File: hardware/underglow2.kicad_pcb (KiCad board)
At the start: 4 copper layers, 6 parts, among them U201 TPS62172DSGR

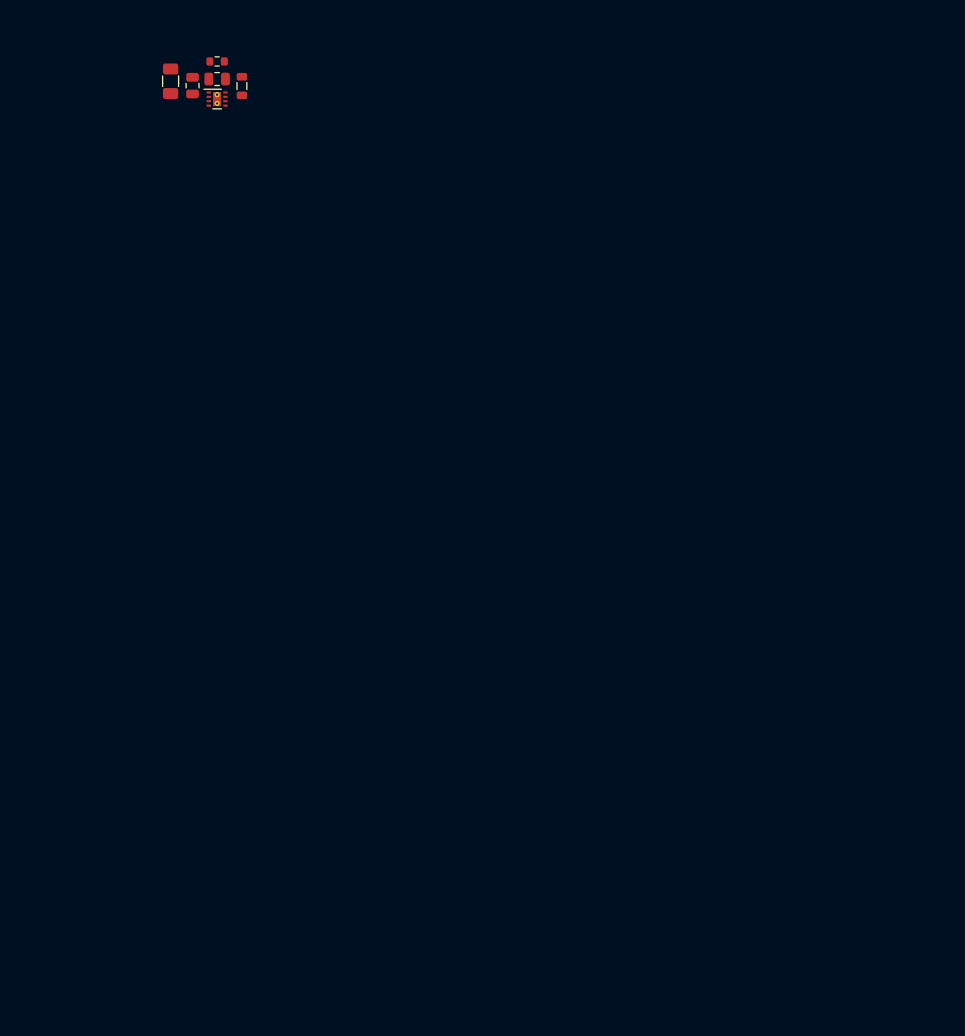
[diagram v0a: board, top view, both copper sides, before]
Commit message: Schematic updates: stm32 sheet
Signed-off-by: Connor Rigby <connorr@hey.com>
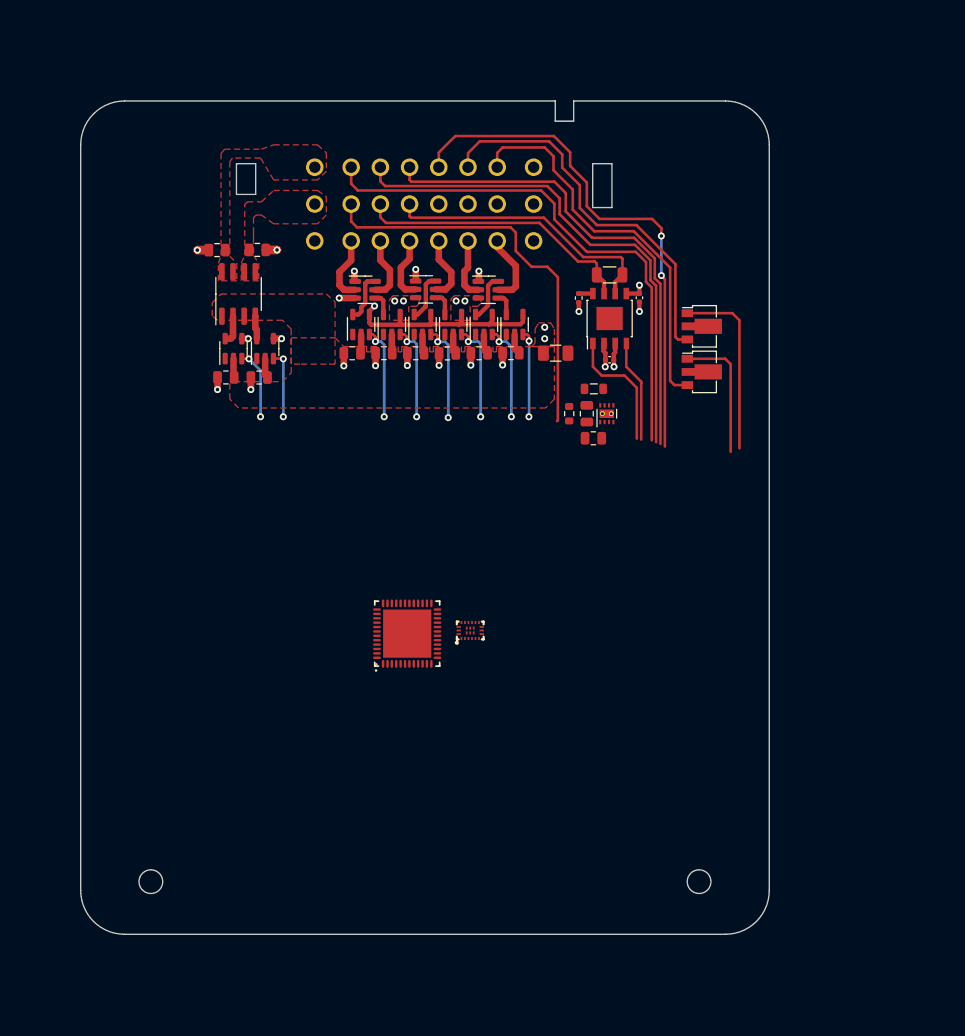
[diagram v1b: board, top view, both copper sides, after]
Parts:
- added C301: C_0805_10u_X5R, Capacitor_SMD:C_0805_2012Metric, F.Cu at (59.6, 53.8)
- added C302: C_0805_10u_X5R, Capacitor_SMD:C_0805_2012Metric, F.Cu at (56.0, 53.8)
- added C303: C_0805_10u_X5R, Capacitor_SMD:C_0805_2012Metric, F.Cu at (66.8, 53.8)
- added C304: C_0805_10u_X5R, Capacitor_SMD:C_0805_2012Metric, F.Cu at (63.2, 53.8)
- added C305: C_0805_10u_X5R, Capacitor_SMD:C_0805_2012Metric, F.Cu at (74.0, 53.8)
- added C306: C_0805_10u_X5R, Capacitor_SMD:C_0805_2012Metric, F.Cu at (70.4, 53.8)
- added C307: C_0805_10u_X5R, Capacitor_SMD:C_0805_2012Metric, F.Cu at (41.5, 56.5)
- added C308: C_0805_10u_X5R, Capacitor_SMD:C_0805_2012Metric, F.Cu at (45.4, 56.5)
- added C309: C_0805_10u_X5R, Capacitor_SMD:C_0805_2012Metric, F.Cu at (40.5, 42.0)
- added C310: C_0805_10u_X5R, Capacitor_SMD:C_0805_2012Metric, F.Cu at (45.1, 42.0)
- added C401: C_0402_100nf_X7R, Capacitor_SMD:C_0402_1005Metric, F.Cu at (85.3, 54.5)
- added C402: C_0402_100nf_X7R, Capacitor_SMD:C_0402_1005Metric, F.Cu at (88.7, 47.4)
- added H1101: MountingHole_Pad, MountingHole:MountingHole_2.7mm_M2.5, F.Cu at (33.0, 114.0)
- added H1102: MountingHole_Pad, MountingHole:MountingHole_2.7mm_M2.5, F.Cu at (95.5, 114.0)
- added J101: J_Delphi_Sicma_24, bom:Delphi_Sicma_24_Black, F.Cu at (64.2, 25.0)
- added Q301: AO4803A, Package_SO:SOP-8_3.76x4.96mm_P1.27mm, F.Cu at (43.0, 47.0)
- added Q302: 8205A, Package_TO_SOT_SMD:SOT-23-6, F.Cu at (57.4, 46.5)
- added Q303: 8205A, Package_TO_SOT_SMD:SOT-23-6, F.Cu at (64.3, 46.5)
- added Q304: 8205A, Package_TO_SOT_SMD:SOT-23-6, F.Cu at (71.5, 46.5)
- added Q305: BCX56, Package_TO_SOT_SMD:SOT-89-3, F.Cu at (95.8, 55.9)
- added Q306: BCX56, Package_TO_SOT_SMD:SOT-89-3, F.Cu at (95.8, 50.7)
- added R401: R_1206_120, Resistor_SMD:R_1206_3216Metric, F.Cu at (85.3, 44.8)
- added R402: R_0402_10k, Resistor_SMD:R_0402_1005Metric, F.Cu at (81.8, 47.5)
- added U301: MCP1416, Package_TO_SOT_SMD:SOT-23-5, F.Cu at (60.5, 50.5)
- added U302: MCP1416, Package_TO_SOT_SMD:SOT-23-5, F.Cu at (57.0, 50.5)
- added U303: MCP1416, Package_TO_SOT_SMD:SOT-23-5, F.Cu at (67.5, 50.5)
- added U304: MCP1416, Package_TO_SOT_SMD:SOT-23-5, F.Cu at (64.0, 50.5)
- added U305: MCP1416, Package_TO_SOT_SMD:SOT-23-5, F.Cu at (74.5, 50.5)
- added U306: MCP1416, Package_TO_SOT_SMD:SOT-23-5, F.Cu at (71.0, 50.5)
- added U307: MCP1416, Package_TO_SOT_SMD:SOT-23-5, F.Cu at (42.4, 53.2)
- added U308: MCP1416, Package_TO_SOT_SMD:SOT-23-5, F.Cu at (46.0, 53.2)
- added U401: TLE9251VSJXUMA1, Package_SO:Infineon_PG-DSO-8-43, F.Cu at (85.3, 49.8)
- added U501: STM32G431CBU6, LCSC_Microcontroller:UFQFPN-48_L7.0-W7.0-P0.50-BL-EP, F.Cu at (62.2, 85.7)
- added U601: DA14531-00000FX2, LCSC_Microcontroller:FCGQFN-24_L3.0-W2.2-P0.40-BL, F.Cu at (69.4, 85.4)
- moved C201 60.9 mm to (83.4, 63.5), turned to 180 degrees
- moved U201 57.1 mm to (85.0, 60.6), turned to 90 degrees
- moved C202 56.9 mm to (82.7, 60.6), turned to -90 degrees
- moved R203 56.8 mm to (80.7, 60.6), turned to -90 degrees
- moved F201 53.7 mm to (79.2, 53.8), turned to 0 degrees
- moved L201 52.9 mm to (83.5, 57.8), turned to 180 degrees
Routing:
- net /Digital Input/DI_1: track 0.00 -> 60.8 mm
- net /Digital Input/DI_4: track 0.00 -> 59.7 mm, vias 0 -> 2
- net /Digital Input/DI_2: track 0.00 -> 58.2 mm
- net /Digital Input/DI_3: track 0.00 -> 55.8 mm
- net GND: track 0.00 -> 50.6 mm, vias 0 -> 24
- net /Power/EN: track 0.00 -> 45.9 mm
- net /RGB/PIXEL_1: track 0.00 -> 44.6 mm
- net /RGB/PIXEL_2: track 0.00 -> 43.8 mm
- net /CAN/CAN_H: track 0.00 -> 32.1 mm
- net /CAN/CAN_L: track 0.00 -> 32.0 mm
- net /Application/PIXEL_2_PWM: track 0.00 -> 20.9 mm
- net +12V: track 0.00 -> 17.9 mm, vias 0 -> 2
- net /Application/PIXEL_1_PWM: track 0.00 -> 15.2 mm
- net /Application/CAN_RX: track 0.00 -> 14.5 mm
- net /Application/CAN_TX: track 0.00 -> 11.7 mm
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- added copper zone on F.Cu, net +12V
- added copper zone on F.Cu, net /RGB/RGB1_12V
- added copper zone on F.Cu, net /RGB/RGB2_12V
- added copper zone on F.Cu, net GND
- added copper zone on In1.Cu, net GND
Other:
- board outline added: 78.5 x 95 mm

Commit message: Schematic and layout Progress
Signed-off-by: Connor Rigby <connorr@hey.com>
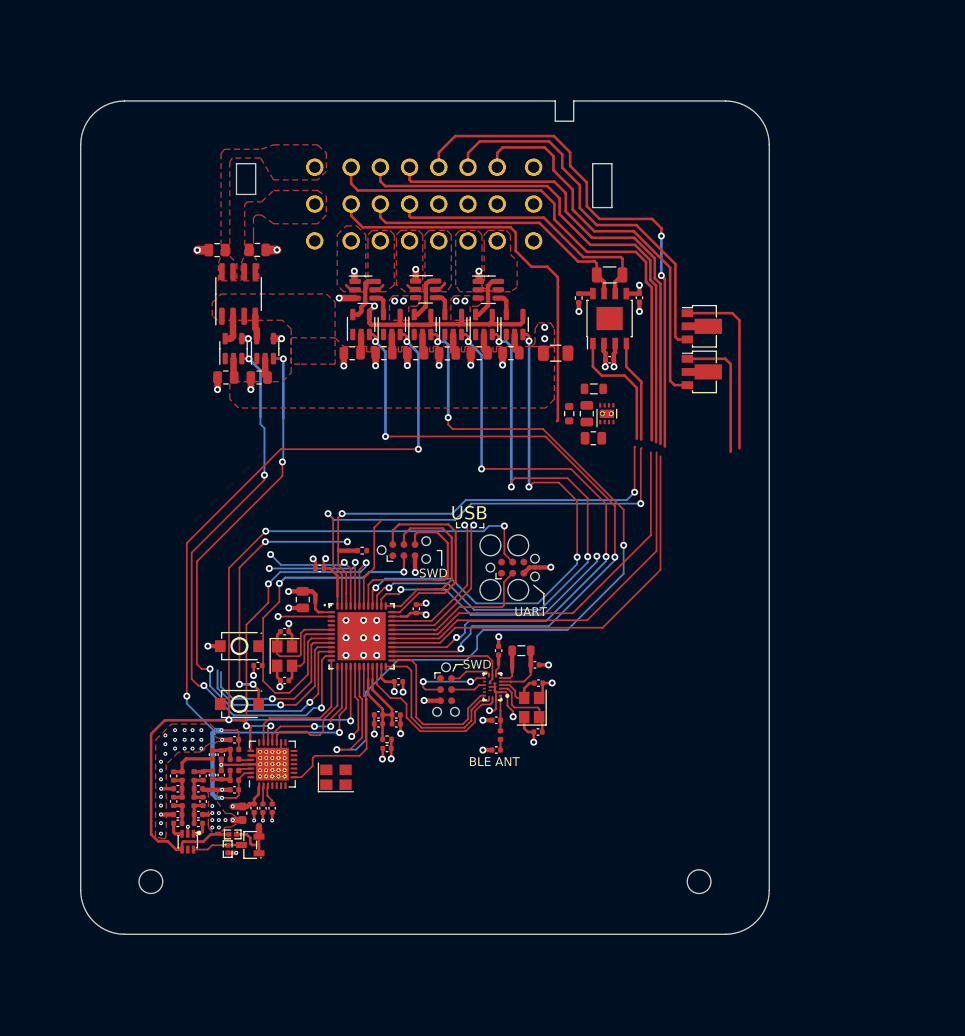
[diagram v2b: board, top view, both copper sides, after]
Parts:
- added BTN501: GT-TC029B-H025-L1N, Button:SW-SMD_L3.9-W3.0-P4.45, F.Cu at (43.1, 87.2)
- added BTN502: GT-TC029B-H025-L1N, Button:SW-SMD_L3.9-W3.0-P4.45, F.Cu at (43.1, 93.8)
- added C402: GJM1555C1H3R3WB01D, Capacitor_SMD:C_0402_1005Metric, F.Cu at (38.4, 106.4)
- added C403: DNP, Capacitor_SMD:C_0402_1005Metric, F.Cu at (39.0, 104.9)
- added C404: GCM1555C1H6R8BA16D, Capacitor_SMD:C_0402_1005Metric, F.Cu at (38.4, 103.4)
- added C405: DNP, Capacitor_SMD:C_0402_1005Metric, F.Cu at (39.0, 102.0)
- added C406: GJM1555C1H220FB01D, Capacitor_SMD:C_0402_1005Metric, F.Cu at (40.0, 101.8)
- added C407: GJM1555C1H8R2BB01D, Capacitor_SMD:C_0402_1005Metric, F.Cu at (41.0, 101.8)
- added C408: C1005X7S2A103KT000F, Capacitor_SMD:C_0402_1005Metric, F.Cu at (42.5, 103.5)
- added C409: GCM1555C1H6R8BA16D, Capacitor_SMD:C_0402_1005Metric, F.Cu at (36.1, 103.4)
- added C410: CL05B104KB54PNC, Capacitor_SMD:C_0402_1005Metric, F.Cu at (44.8, 105.6)
- added C411: CL05B104KB54PNC, Capacitor_SMD:C_0402_1005Metric, F.Cu at (45.8, 105.6)
- added C412: CL05B104KB54PNC, Capacitor_SMD:C_0402_1005Metric, F.Cu at (46.8, 105.6)
- added C415: CC0402JRNPO9BN101, Capacitor_SMD:C_0402_1005Metric, F.Cu at (38.4, 107.4)
- added C416: CGA2B2NP01H680JT0Y0F, Capacitor_SMD:C_0402_1005Metric, F.Cu at (42.5, 97.8)
- added C417: GCM1555C1H4R7BA16D, Capacitor_SMD:C_0402_1005Metric, F.Cu at (41.0, 99.5)
- added C418: GJM1555C1H8R2BB01D, Capacitor_SMD:C_0402_1005Metric, F.Cu at (40.0, 99.5)
- added C419: DNP, Capacitor_SMD:C_0402_1005Metric, F.Cu at (35.6, 102.0)
- added C421: DNP, Capacitor_SMD:C_0402_1005Metric, F.Cu at (35.6, 104.9)
- added C422: GCM1555C1H5R6BA16D, Capacitor_SMD:C_0402_1005Metric, F.Cu at (36.1, 106.4)
- added C423: CC0402JRNPO9BN101, Capacitor_SMD:C_0402_1005Metric, F.Cu at (36.1, 107.4)
- added C425: GRM188Z71A106KA73D, Capacitor_SMD:C_0603_1608Metric, F.Cu at (43.4, 106.2)
- added C503: C_0402_DNP, Capacitor_SMD:C_0402_1005Metric, F.Cu at (48.2, 85.5)
- added C504: C_0402_DNP, Capacitor_SMD:C_0402_1005Metric, F.Cu at (48.2, 91.1)
- added C505: C_0402_100nf_X7R, Capacitor_SMD:C_0402_1005Metric, F.Cu at (45.2, 89.4)
- added C506: C_0402_1u_X5R, Capacitor_SMD:C_0402_1005Metric, F.Cu at (58.9, 95.0)
- added C507: C_0402_100nf_X7R, Capacitor_SMD:C_0402_1005Metric, F.Cu at (58.9, 96.0)
- added C508: C_0402_100nf_X7R, Capacitor_SMD:C_0402_1005Metric, F.Cu at (59.9, 98.8)
- added C50823: C_0402_100nf_X7R, Capacitor_SMD:C_0402_1005Metric, F.Cu at (61.2, 91.2)
- added C50835: C_0402_100nf_X7R, Capacitor_SMD:C_0402_1005Metric, F.Cu at (63.3, 82.9)
- added C50848: C_0402_100nf_X7R, Capacitor_SMD:C_0402_1005Metric, F.Cu at (52.2, 78.3)
- added C509: C_0805_10u_X5R, Capacitor_SMD:C_0805_2012Metric, F.Cu at (50.3, 81.8)
- added C510: C_0402_1u_X5R, Capacitor_SMD:C_0402_1005Metric, F.Cu at (61.0, 96.0)
- added C511: C_0402_100nf_X7R, Capacitor_SMD:C_0402_1005Metric, F.Cu at (61.0, 95.0)
- added C601: C_0402_2u2_X75R, Capacitor_SMD:C_0402_1005Metric, F.Cu at (72.7, 87.7)
- added C602: C_0402_4u7_X5R, Capacitor_SMD:C_0402_1005Metric, F.Cu at (76.8, 89.3)
- added C603: C_0402_DNP, Capacitor_SMD:C_0402_1005Metric, F.Cu at (77.2, 91.4)
- added C604: C_0402_DNP, Capacitor_SMD:C_0402_1005Metric, F.Cu at (77.1, 96.9)
- added C6Z1: C_0402_1p8_C0G, Capacitor_SMD:C_0402_1005Metric, F.Cu at (72.4, 95.6)
- added C6Z3: C_0402_1p8_C0G, Capacitor_SMD:C_0402_1005Metric, F.Cu at (72.4, 99.0)
- added J501: Conn_ARM_SWD_TagConnect_TC2030-NL, Connector:Tag-Connect_TC2030-IDC-NL_2x03_P1.27mm_Vertical, F.Cu at (61.9, 76.2)
- added J502: Conn_ARM_SWD_TagConnect_TC2030, Connector:Tag-Connect_TC2030-IDC-FP_2x03_P1.27mm_Vertical, F.Cu at (74.2, 78.2)
- added J601: Conn_ARM_SWD_TagConnect_TC2030-NL, Connector:Tag-Connect_TC2030-IDC-NL_2x03_P1.27mm_Vertical, F.Cu at (66.7, 92.1)
- added L401: LQW15AN5N6C10D, Inductor_SMD:L_0402_1005Metric, F.Cu at (37.9, 104.9)
- added L402: LQW15AN5N6C10D, Inductor_SMD:L_0402_1005Metric, F.Cu at (37.9, 102.0)
- added L403: LQW15AN22NG00D, Inductor_SMD:L_0402_1005Metric, F.Cu at (42.5, 102.4)
- added L404: MLK1005S2N7ST000, Inductor_SMD:L_0402_1005Metric, F.Cu at (42.5, 101.3)
- added L405: LQP15MN3N9B02D, Inductor_SMD:L_0402_1005Metric, F.Cu at (42.5, 100.0)
- added L406: LQW15AN33NH00D, Inductor_SMD:L_0402_1005Metric, F.Cu at (42.5, 98.9)
- added L407: LQW15AN6N8J00D, Inductor_SMD:L_0402_1005Metric, F.Cu at (36.6, 102.0)
- added L408: LQW15AN6N8J00D, Inductor_SMD:L_0402_1005Metric, F.Cu at (36.6, 104.9)
- added L501: R_0402_DNP, Resistor_SMD:R_0402_1005Metric, F.Cu at (59.9, 97.8)
- added L601: L_0805_2u2, Inductor_SMD:L_0805_2012Metric, F.Cu at (75.2, 87.7)
- added L6Z2: L_0402_3n3, Inductor_SMD:L_0402_1005Metric, F.Cu at (72.9, 97.3)
- added NT601: NetTie_2, NetTie:NetTie-2_SMD_Pad0.5mm, F.Cu at (55.0, 76.3)
- added Q401: FMMT491_C5278003, easyeda:SOT-23-3_L2.9-W1.3-P1.90-LS2.4-BR, F.Cu at (44.3, 109.8)
- added R401: PTFR0402B1K00P9, easyeda:R0402, F.Cu at (41.8, 110.3)
- added R402: PTFR0402B1K00P9, easyeda:R0402, F.Cu at (42.3, 108.6)
- added R502: R_0402_10k, Resistor_SMD:R_0402_1005Metric, F.Cu at (57.1, 76.3)
- added U402: XA17-G4K, easyeda:SOT-363_L2.0-W1.3-P0.65-LS2.1-BR, F.Cu at (37.2, 109.4)
- added U801: RF69, Package_DFN_QFN:QFN-28-1EP_5x5mm_P0.5mm_EP3.75x3.75mm_ThermalVias, F.Cu at (46.8, 100.6)
- added Y501: 32_Mhz, Crystal:Crystal_SMD_3225-4Pin_3.2x2.5mm, F.Cu at (48.2, 88.3)
- added Y601: 32_Mhz, Crystal:Crystal_SMD_3225-4Pin_3.2x2.5mm, F.Cu at (76.4, 94.2)
- added Y801: 32_Mhz, Crystal:Crystal_SMD_3225-4Pin_3.2x2.5mm, F.Cu at (54.1, 102.1)
- moved U601 6.90 mm to (71.9, 91.8), turned to 90 degrees
- moved U501 5.21 mm to (57.0, 86.0), turned to -90 degrees
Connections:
- U501 pad 1: unconnected-(U501-Pad1) -> +3.3V
- U501 pad 10: unconnected-(U501-Pad10) -> /Application/RGB2_EN
- U501 pad 11: unconnected-(U501-Pad11) -> /Application/RGB1_EN
- U501 pad 12: unconnected-(U501-Pad12) -> /Application/SPI1_NSS
- U501 pad 13: unconnected-(U501-Pad13) -> /Application/SPI1_SCK
- U501 pad 14: unconnected-(U501-Pad14) -> /Application/SPI1_MISO
- U501 pad 15: unconnected-(U501-Pad15) -> /Application/RGB1_R_PWM
- U501 pad 16: unconnected-(U501-Pad16) -> /Application/USART1_TX
- U501 pad 18: unconnected-(U501-Pad18) -> /Application/RGB2_R_PWM
- U501 pad 19: unconnected-(U501-Pad19) -> /Application/SPI1_IRQ
- U501 pad 20: unconnected-(U501-Pad20) -> +3.3VA
- U501 pad 21: unconnected-(U501-Pad21) -> +3.3VA
- U501 pad 22: unconnected-(U501-Pad22) -> /Application/LPUART1_RX
- U501 pad 23: unconnected-(U501-Pad23) -> +3.3V
- U501 pad 24: unconnected-(U501-Pad24) -> /Application/LPUART1_TX
- U501 pad 25: unconnected-(U501-Pad25) -> /Application/LPUART1_RTS
- U501 pad 26: unconnected-(U501-Pad26) -> /Application/LPUART1_CTS
- U501 pad 27: unconnected-(U501-Pad27) -> /Application/RGB1_G_PWM
- U501 pad 28: unconnected-(U501-Pad28) -> /Application/RGB1_B_PWM
- U501 pad 29: unconnected-(U501-Pad29) -> /Application/DI3_TTL
- U501 pad 30: unconnected-(U501-Pad30) -> /Application/DI2_TTL
- U501 pad 31: unconnected-(U501-Pad31) -> /Application/DI1_TTL
- U501 pad 32: unconnected-(U501-Pad32) -> /Application/USART1_RX
- U501 pad 33: unconnected-(U501-Pad33) -> /Application/USB_DN
- U501 pad 34: unconnected-(U501-Pad34) -> /Application/USB_DP
- U501 pad 35: unconnected-(U501-Pad35) -> +3.3V
- U501 pad 36: unconnected-(U501-Pad36) -> /Application/SWDIO
- U501 pad 37: unconnected-(U501-Pad37) -> /Application/SWCLK
- U501 pad 39: unconnected-(U501-Pad39) -> /Application/RGB2_B_PWM
- U501 pad 40: unconnected-(U501-Pad40) -> /Application/RGB2_G_PWM
- U501 pad 41: unconnected-(U501-Pad41) -> /Application/SWO
- U501 pad 43: unconnected-(U501-Pad43) -> /Application/SPI1_MOSI
- U501 pad 46: unconnected-(U501-Pad46) -> /Application/CAN_RX
- U501 pad 47: unconnected-(U501-Pad47) -> /Application/CAN_TX
- U501 pad 48: unconnected-(U501-Pad48) -> +3.3V
- U501 pad 5: unconnected-(U501-Pad5) -> /Application/HSE_IN
- U501 pad 6: unconnected-(U501-Pad6) -> /Application/HSE_OUT
- U501 pad 7: unconnected-(U501-Pad7) -> /Application/~{RST}
- U601 pad 1: unconnected-(U601-Pad1) -> /BLE/RFIOp
- U601 pad 10: unconnected-(U601-Pad10) -> /BLE/RST
- U601 pad 12: unconnected-(U601-Pad12) -> /BLE/SWCLK
- U601 pad 15: unconnected-(U601-Pad15) -> /Application/LPUART1_RTS
- U601 pad 16: unconnected-(U601-Pad16) -> /Application/LPUART1_TX
- U601 pad 17: unconnected-(U601-Pad17) -> /Application/LPUART1_RX
- U601 pad 18: unconnected-(U601-Pad18) -> GND
- U601 pad 19: unconnected-(U601-Pad19) -> GND
- U601 pad 2: unconnected-(U601-Pad2) -> GND
- U601 pad 20: unconnected-(U601-Pad20) -> GND
- U601 pad 21: unconnected-(U601-Pad21) -> GND
- U601 pad 22: unconnected-(U601-Pad22) -> /Application/LPUART1_CTS
- U601 pad 23: unconnected-(U601-Pad23) -> GND
- U601 pad 3: unconnected-(U601-Pad3) -> /BLE/XTAL32MP
- U601 pad 4: unconnected-(U601-Pad4) -> /BLE/XTAL32Mm
- U601 pad 5: unconnected-(U601-Pad5) -> /BLE/BAT_LOW
- U601 pad 6: unconnected-(U601-Pad6) -> /BLE/LX
- U601 pad 7: unconnected-(U601-Pad7) -> /BLE/VBAT_HIGH
- U601 pad 8: unconnected-(U601-Pad8) -> /Application/LPUART1_CTS
- U601 pad 9: unconnected-(U601-Pad9) -> /BLE/SWDIO
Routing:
- net (no net): track 0.00 -> 93.7 mm, vias 0 -> 2
- net /Application/RGB2_R_PWM: track 11.2 -> 100.6 mm, vias 2 -> 4
- net GND: track 50.6 -> 136.7 mm, vias 24 -> 95
- net /Application/RGB1_R_PWM: track 11.0 -> 90.0 mm, vias 2 -> 4
- net /Application/USART1_TX: track 0.00 -> 75.3 mm, vias 0 -> 4
- net /Application/RGB1_G_PWM: track 10.7 -> 78.7 mm, vias 2 -> 4
- net /Application/RGB1_EN: track 7.97 -> 65.1 mm, vias 2 -> 4
- net /Application/RGB1_B_PWM: track 11.3 -> 67.9 mm, vias 2 -> 4
- net /Application/RGB2_EN: track 7.73 -> 64.2 mm, vias 2 -> 4
- net /Application/RGB2_B_PWM: track 11.1 -> 66.1 mm, vias 2 -> 4
- net /Application/CAN_TX: track 11.7 -> 65.9 mm, vias 0 -> 2
- net /Application/CAN_RX: track 14.5 -> 65.7 mm, vias 0 -> 2
- net /Application/RGB2_G_PWM: track 9.97 -> 60.4 mm, vias 2 -> 4
- net /Application/DI3_TTL: track 0.00 -> 47.0 mm
- net /Application/DI2_TTL: track 0.00 -> 45.6 mm
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- added copper zone on F.Cu, net /RGB/RGB1_B
- added copper zone on F.Cu, net /RGB/RGB1_G
- added copper zone on F.Cu, net /RGB/RGB1_R
- added copper zone on F.Cu, net /RGB/RGB2_B
- added copper zone on F.Cu, net /RGB/RGB2_G
- added copper zone on F.Cu, net /RGB/RGB2_R
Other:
- board text added: "BLE ANT"
- board text added: "SWD"
- board text added: "UART"
- board text added: "USB"

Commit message: Layout updates
Signed-off-by: Connor Rigby <connorr@hey.com>
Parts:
- removed the C402 at (38.4, 106.4)
- removed C403, C405, C419, C421: DNP, Capacitor_SMD:C_0402_1005Metric
- removed C404, C409: GCM1555C1H6R8BA16D, Capacitor_SMD:C_0402_1005Metric
- removed C406: GJM1555C1H220FB01D, Capacitor_SMD:C_0402_1005Metric
- removed C407, C418: GJM1555C1H8R2BB01D, Capacitor_SMD:C_0402_1005Metric
- removed C408: C1005X7S2A103KT000F, Capacitor_SMD:C_0402_1005Metric
- removed C410, C411, C412: CL05B104KB54PNC, Capacitor_SMD:C_0402_1005Metric
- removed C415, C423: CC0402JRNPO9BN101, Capacitor_SMD:C_0402_1005Metric
- removed C416: CGA2B2NP01H680JT0Y0F, Capacitor_SMD:C_0402_1005Metric
- removed C417: GCM1555C1H4R7BA16D, Capacitor_SMD:C_0402_1005Metric
- removed C422: GCM1555C1H5R6BA16D, Capacitor_SMD:C_0402_1005Metric
- removed C425: GRM188Z71A106KA73D, Capacitor_SMD:C_0603_1608Metric
- removed L401, L402: LQW15AN5N6C10D, Inductor_SMD:L_0402_1005Metric
- removed L403: LQW15AN22NG00D, Inductor_SMD:L_0402_1005Metric
- removed L404: MLK1005S2N7ST000, Inductor_SMD:L_0402_1005Metric
- removed L405: LQP15MN3N9B02D, Inductor_SMD:L_0402_1005Metric
- removed L406: LQW15AN33NH00D, Inductor_SMD:L_0402_1005Metric
- removed L407, L408: LQW15AN6N8J00D, Inductor_SMD:L_0402_1005Metric
- removed Q401: FMMT491_C5278003, easyeda:SOT-23-3_L2.9-W1.3-P1.90-LS2.4-BR
- removed the R401 at (41.8, 110.3)
- removed the R402 at (42.3, 108.6)
- removed U402: XA17-G4K, easyeda:SOT-363_L2.0-W1.3-P0.65-LS2.1-BR
- added C701: C_0603_DNP, Capacitor_SMD:C_0603_1608Metric, F.Cu at (98.4, 84.8)
- added C702: C_0603_DNP, Capacitor_SMD:C_0603_1608Metric, F.Cu at (95.2, 84.8)
- added C703: C_0603_DNP, Capacitor_SMD:C_0603_1608Metric, F.Cu at (92.0, 84.8)
- added C704: C_0603_DNP, Capacitor_SMD:C_0603_1608Metric, F.Cu at (88.8, 84.8)
- added C801: C_0402_DNP, Capacitor_SMD:C_0402_1005Metric, F.Cu at (36.0, 95.5)
- added C810: C_0402_100nf_X7R, Capacitor_SMD:C_0402_1005Metric, F.Cu at (33.8, 88.7)
- added C811: C_0402_100nf_X7R, Capacitor_SMD:C_0402_1005Metric, F.Cu at (33.8, 89.9)
- added C812: C_0402_100nf_X7R, Capacitor_SMD:C_0402_1005Metric, F.Cu at (33.8, 91.1)
- added C813: C_0402_DNP, Capacitor_SMD:C_0402_1005Metric, F.Cu at (31.5, 95.5)
- added C815: C_0402_100nf_X7R, Capacitor_SMD:C_0402_1005Metric, F.Cu at (44.2, 94.0)
- added R501: R_0402_1k, Resistor_SMD:R_0402_1005Metric, F.Cu at (61.3, 69.7)
- added R701: DNP, Resistor_SMD:R_0603_1608Metric, F.Cu at (95.2, 80.8)
- added R702: DNP, Resistor_SMD:R_0603_1608Metric, F.Cu at (98.4, 83.2)
- added R703: DNP, Resistor_SMD:R_0603_1608Metric, F.Cu at (93.6, 80.8)
- added R704: DNP, Resistor_SMD:R_0603_1608Metric, F.Cu at (95.2, 83.2)
- added R705: DNP, Resistor_SMD:R_0603_1608Metric, F.Cu at (92.0, 80.8)
- added R706: DNP, Resistor_SMD:R_0603_1608Metric, F.Cu at (92.0, 83.2)
- added R707: DNP, Resistor_SMD:R_0603_1608Metric, F.Cu at (90.4, 80.8)
- added R708: DNP, Resistor_SMD:R_0603_1608Metric, F.Cu at (88.8, 83.2)
- added TP201: 3.3v, TestPoint:TestPoint_Pad_D1.0mm, F.Cu at (80.6, 58.2)
- added TP202: GND, TestPoint:TestPoint_Pad_D1.0mm, F.Cu at (80.6, 63.6)
- added TP501: DP, TestPoint:TestPoint_Pad_D1.0mm, F.Cu at (73.5, 68.0)
- added TP502: DN, TestPoint:TestPoint_Pad_D1.0mm, F.Cu at (75.5, 68.0)
- added TP503: GND, TestPoint:TestPoint_Pad_D1.0mm, F.Cu at (77.6, 68.0)
- U501: footprint LCSC_Microcontroller:UFQFPN-48_L7.0-W7.0-P0.50-BL-EP -> LCSC_Microcontroller:QFN50P700X700X60-49N
- moved Y801 21.9 mm to (33.8, 94.0), turned to -90 degrees
- moved U801 10.6 mm to (40.3, 92.3), turned to 0 degrees
- moved C602 8.85 mm to (82.8, 82.8), turned to -90 degrees
- moved R502 8.50 mm to (62.5, 69.7), turned to 90 degrees
- moved C508 7.48 mm to (65.0, 93.3)
- moved L501 7.48 mm to (65.0, 92.3)
- moved U501 7.00 mm to (62.0, 81.1), turned to 0 degrees
- moved C50835 6.98 mm to (68.2, 78.0)
- moved BTN501 6.98 mm to (48.1, 82.2)
- moved BTN502 6.98 mm to (48.1, 88.8)
- moved C503 6.98 mm to (53.2, 80.6)
- moved C504 6.98 mm to (53.2, 86.2)
- moved C505 6.98 mm to (50.2, 84.5)
- moved C506 6.98 mm to (63.9, 90.1)
- moved C507 6.98 mm to (63.9, 91.1)
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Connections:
- BTN502 pad 1: unconnected-(BTN502-Pad1) -> /Application/BOOT0
- BTN502 pad 2: unconnected-(BTN502-Pad2) -> Net-(BTN502-Pad2)
- C202 pad 1: +VSW -> +3.3V
- C601 pad 1: /BLE/VBAT_HIGH -> +3.3V
- L201 pad 2: +VSW -> +3.3V
- R203 pad 1: +VSW -> +3.3V
- R502 pad 2: unconnected-(R502-Pad2) -> GND
- U201 pad 6: +VSW -> +3.3V
- U501 pad 17: unconnected-(U501-Pad17) -> /Application/SPI1_RESET
- U501 pad 29: /Application/DI3_TTL -> /Application/DI1_TTL
- U501 pad 31: /Application/DI1_TTL -> /Application/DI3_TTL
- U501 pad 38: unconnected-(U501-Pad38) -> /Application/DI4_TTL
- U501 pad 42: unconnected-(U501-Pad42) -> /Application/PIXEL_1_PWM
- U601 pad 7: /BLE/VBAT_HIGH -> +3.3V
- U801 pad 1: unconnected-(U801-Pad1) -> +3.3V
- U801 pad 15: unconnected-(U801-Pad15) -> +3.3V
- U801 pad 2: unconnected-(U801-Pad2) -> /Radio/VR_ANA
- U801 pad 3: unconnected-(U801-Pad3) -> /Radio/VR_DIG
- U801 pad 4: unconnected-(U801-Pad4) -> /Radio/XTA
- U801 pad 5: unconnected-(U801-Pad5) -> /Radio/XTB
- Y801 pad 1: unconnected-(Y801-Pad1) -> /Radio/XTA
- Y801 pad 2: unconnected-(Y801-Pad2) -> GND
- Y801 pad 3: unconnected-(Y801-Pad3) -> /Radio/XTB
- Y801 pad 4: unconnected-(Y801-Pad4) -> GND
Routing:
- net +3.3V: track 35.4 -> 220.8 mm, vias 9 -> 17
- net (no net): track 93.7 -> 0.00 mm, vias 2 -> 0
- net /Application/PIXEL_2_PWM: track 20.9 -> 88.3 mm, vias 0 -> 1
- net +12V: track 17.9 -> 74.2 mm, vias 2 -> 6
- net /Application/PIXEL_1_PWM: track 15.2 -> 68.6 mm, vias 0 -> 2
- net /Application/SPI1_RESET: track 0.00 -> 39.6 mm, vias 0 -> 2
- net /Application/BOOT0: track 1.07 -> 40.5 mm, vias 0 -> 2
- net /RGB/RGB1_12V: track 0.00 -> 38.8 mm
- net /RGB/RGB2_12V: track 0.00 -> 37.1 mm
- net /Application/DI4_TTL: track 0.00 -> 35.4 mm, vias 0 -> 2
- net Net-(BTN502-Pad2): track 0.00 -> 35.1 mm, vias 0 -> 4
- net unconnected-(BTN502-Pad2): track 30.9 -> 0.00 mm, vias 4 -> 0
- net unconnected-(U501-Pad38): track 30.3 -> 0.00 mm, vias 2 -> 0
- net /Digital Input/DI_4: track 59.7 -> 80.3 mm
- net /Power/VIN: track 0.00 -> 20.2 mm
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- added copper zone on B.Cu, net +3.3V
- added copper zone on F.Cu, net +3.3V
- added copper zone on In2.Cu, net +3.3V
- added copper zone on F.Cu, net /Power/SW
- added copper zone on B.Cu, net GND
- added copper zone on In2.Cu, net GND
- removed copper zone on F.Cu, net /RGB/RGB1_12V
- removed copper zone on F.Cu, net /RGB/RGB2_12V
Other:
- board text removed: "BLE ANT"
- board text removed: "SWD"
- board text removed: "UART"
- board text removed: "USB"
